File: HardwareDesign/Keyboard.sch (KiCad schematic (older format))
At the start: 13 parts, among them J501 Conn_01x20, U501 87C51/89C51, U502 IDT7201, U503 74HCT138, U504 74HCT541, Y501 11.0592 MHz

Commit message: more preparations for PCB layout
More nets connected to appropriate backplane connector pin.
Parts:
- removed RN501: 4k7, Resistors_THT:R_Array_SIP10, symbol device:R_Network09
- added J502: Conn_02x40_Counter_Clockwise, symbol Connector_Generic:Conn_02x40_Counter_Clockwise
- added J503: Conn_01x02, symbol Connector_Generic:Conn_01x02
- added RN501: R_Network08, Resistors_THT:R_Array_SIP9, symbol device:R_Network08
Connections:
- net labels added: A1, A10, A11, A12, A13, A14, A15, A2, A3, A4, A5, A6, A7, A8, A9, E, PC0, PC1, PC2, PC3, PC4, PC5, PC6, PC7, R~W, TIRQ, ~IODEV0, ~IODEV1, ~IODEV10, ~IODEV11, ~IODEV12, ~IODEV13, ~IODEV14, ~IODEV15, ~IODEV2, ~IODEV3, ~IODEV4, ~IODEV5, ~IODEV6, ~IODEV7, ~IODEV8, ~IODEV9, ~IOR1~, ~IOR2~, ~IOR3~, ~IOR4~, ~IOR5~, ~IOR6~, ~IOR7~, ~IRQ, ~KIRQ~, ~RMEM~, ~ROMEN~, ~RST~, ~WMEM~
- wire segments 174 -> 261
- no-connect marks 5 -> 4
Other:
- note added: "Jumper to enable keyboard\nIRQ (when FIFO is not empty)"
- note added: "The exact value of RN501 isn't\ncritical: anything between 2k7\nand 47k should work fine."
- note added: "back row (backplane)\nbottom row (board)"
- note added: "backplane connector"
- note added: "front row (backplane)\ntop row (board)"
- note removed: "Note that RN501 could also be\na 9 pin (8 resistor) network.\nThe exact value isn't critical:\nanything between 2k7 and 47k\nshould work fine."
- moved on the sheet: C501, C502, C503, C504, C505, C506, J501, U501, U502, U503, U504, Y501

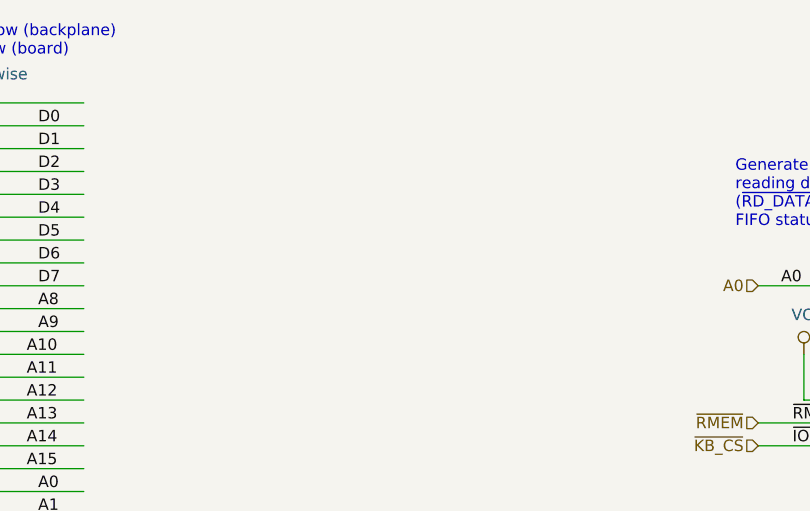
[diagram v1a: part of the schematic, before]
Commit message: more preparations for PCB layout
Make sure all nets connected to backplane connector pins are
labeled correctly.

Add bulk decoupling caps for each backplane connector.

Make keyboard interrupt be -IRQ5 rather than -IRQ7.
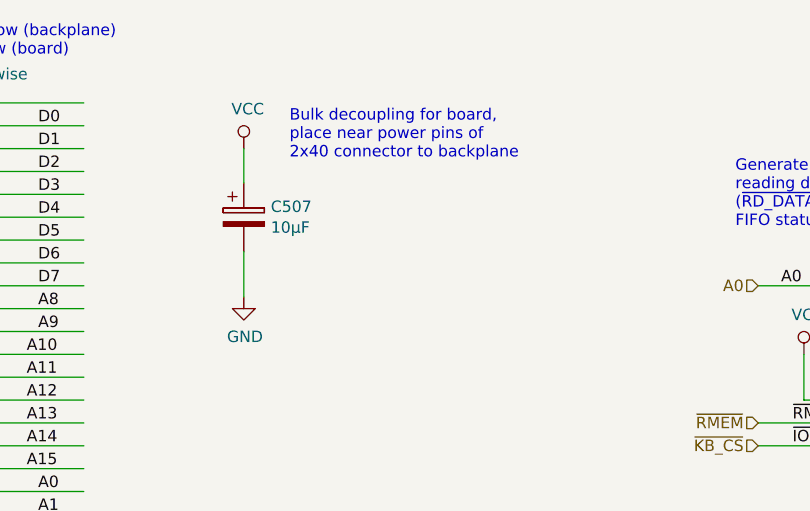
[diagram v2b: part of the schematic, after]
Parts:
- added C507: 10μF, symbol device:CP
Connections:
- wire segments 261 -> 263
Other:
- note added: "Bulk decoupling for board,\nplace near power pins of\n2x40 connector to backplane"
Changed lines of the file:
@@
 Text Label 10850 1250 0    50   ~ 0
 ~KIRQ~
+Text HLabel 11350 1250 2    50   Output ~ 0
+~KIRQ~
+Text Notes 10300 900  0    50   ~ 0
+Jumper to enable keyboard\nIRQ (when FIFO is not empty)
+$Comp
+L device:CP C?
+U 1 1 60CF49C0
+P 3200 1400
+AR Path="/5CFA6AAA/60CF49C0" Ref="C?"  Part="1"
+AR Path="/5E2CF983/60CF49C0" Ref="C507"  Part="1"
+F 0 "C507" H 3318 1446 50  0000 L CNN
+F 1 "10μF" H 3318 1355 50  0000 L CNN
+F 2 "" H 3238 1250 50  0001 C CNN
+F 3 "" H 3200 1400 50  0001 C CNN
+	1    3200 1400
+	1    0    0    -1
+$EndComp
+Wire Wire Line
+	3200 1250 3200 1100
+$Comp
+L power:VCC #PWR?
+U 1 1 60CF49C7
+P 3200 1100
+F 0 "#PWR?" H 3200 950 50  0001 C CNN
+F 1 "VCC" H 3217 1273 50  0000 C CNN
+F 2 "" H 3200 1100 50  0001 C CNN
+F 3 "" H 3200 1100 50  0001 C CNN
+	1    3200 1100
+	1    0    0    -1
+$EndComp
+Wire Wire Line
+	3200 1550 3200 1750
+$Comp
+L power:GND #PWR?
+U 1 1 60CF49CE
+P 3200 1750
+F 0 "#PWR?" H 3200 1500 50  0001 C CNN
+F 1 "GND" H 3205 1577 50  0000 C CNN
+F 2 "" H 3200 1750 50  0001 C CNN
+F 3 "" H 3200 1750 50  0001 C CNN
+	1    3200 1750
+	1    0    0    -1
+$EndComp
+Text Notes 3400 1150 0    50   ~ 0
+Bulk decoupling for board,\nplace near power pins of\n2x40 connector to backplane
 Wire Bus Line
 	8250 1950 8250 5300
 Wire Bus Line
 	10900 1950 10900 6950
-Text HLabel 11350 1250 2    50   Output ~ 0
-~KIRQ~
-Text Notes 10300 900  0    50   ~ 0
-Jumper to enable keyboard\nIRQ (when FIFO is not empty)
 $EndSCHEMATC

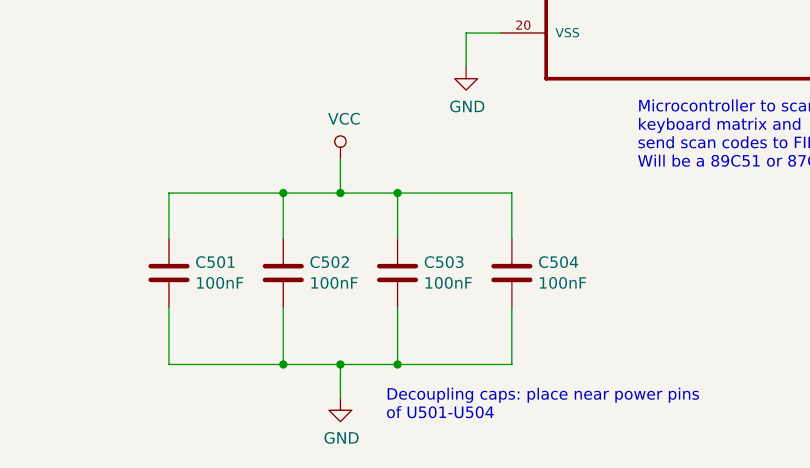
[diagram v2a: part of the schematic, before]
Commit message: a few more consistency tweaks before PCB layout
Routed second timer/counter output to backplane connector,
just in case we want to use it for something eventually
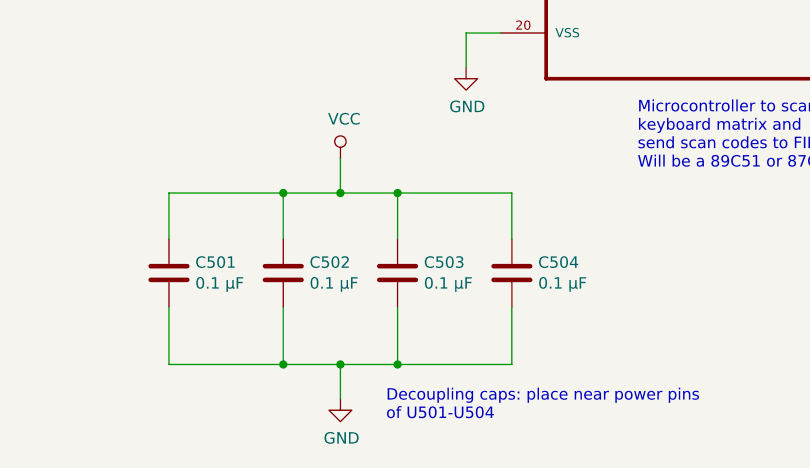
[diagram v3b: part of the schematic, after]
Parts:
- C501, C502, C503, C504: value 100nF -> 0.1 μF
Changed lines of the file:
@@
 P 3450 7950
 F 0 "C501" H 3565 7996 50  0000 L CNN
-F 1 "100nF" H 3565 7905 50  0000 L CNN
+F 1 "0.1 μF" H 3565 7905 50  0000 L CNN
 F 2 "" H 3488 7800 50  0001 C CNN
 F 3 "" H 3450 7950 50  0001 C CNN
@@
 P 3950 7950
 F 0 "C502" H 4065 7996 50  0000 L CNN
-F 1 "100nF" H 4065 7905 50  0000 L CNN
+F 1 "0.1 μF" H 4065 7905 50  0000 L CNN
 F 2 "" H 3988 7800 50  0001 C CNN
 F 3 "" H 3950 7950 50  0001 C CNN
@@
 P 4450 7950
 F 0 "C503" H 4565 7996 50  0000 L CNN
-F 1 "100nF" H 4565 7905 50  0000 L CNN
+F 1 "0.1 μF" H 4565 7905 50  0000 L CNN
 F 2 "" H 4488 7800 50  0001 C CNN
 F 3 "" H 4450 7950 50  0001 C CNN
@@
 P 4950 7950
 F 0 "C504" H 5065 7996 50  0000 L CNN
-F 1 "100nF" H 5065 7905 50  0000 L CNN
+F 1 "0.1 μF" H 5065 7905 50  0000 L CNN
 F 2 "" H 4988 7800 50  0001 C CNN
 F 3 "" H 4950 7950 50  0001 C CNN
@@
 U 1 1 60CF49C7
 P 3200 1100
+AR Path="/5CFA6AAA/60CF49C7" Ref="#PWR?"  Part="1"
+AR Path="/5E2CF983/60CF49C7" Ref="#PWR?"  Part="1"
 F 0 "#PWR?" H 3200 950 50  0001 C CNN
 F 1 "VCC" H 3217 1273 50  0000 C CNN
@@
 U 1 1 60CF49CE
 P 3200 1750
+AR Path="/5CFA6AAA/60CF49CE" Ref="#PWR?"  Part="1"
+AR Path="/5E2CF983/60CF49CE" Ref="#PWR?"  Part="1"
 F 0 "#PWR?" H 3200 1500 50  0001 C CNN
 F 1 "GND" H 3205 1577 50  0000 C CNN

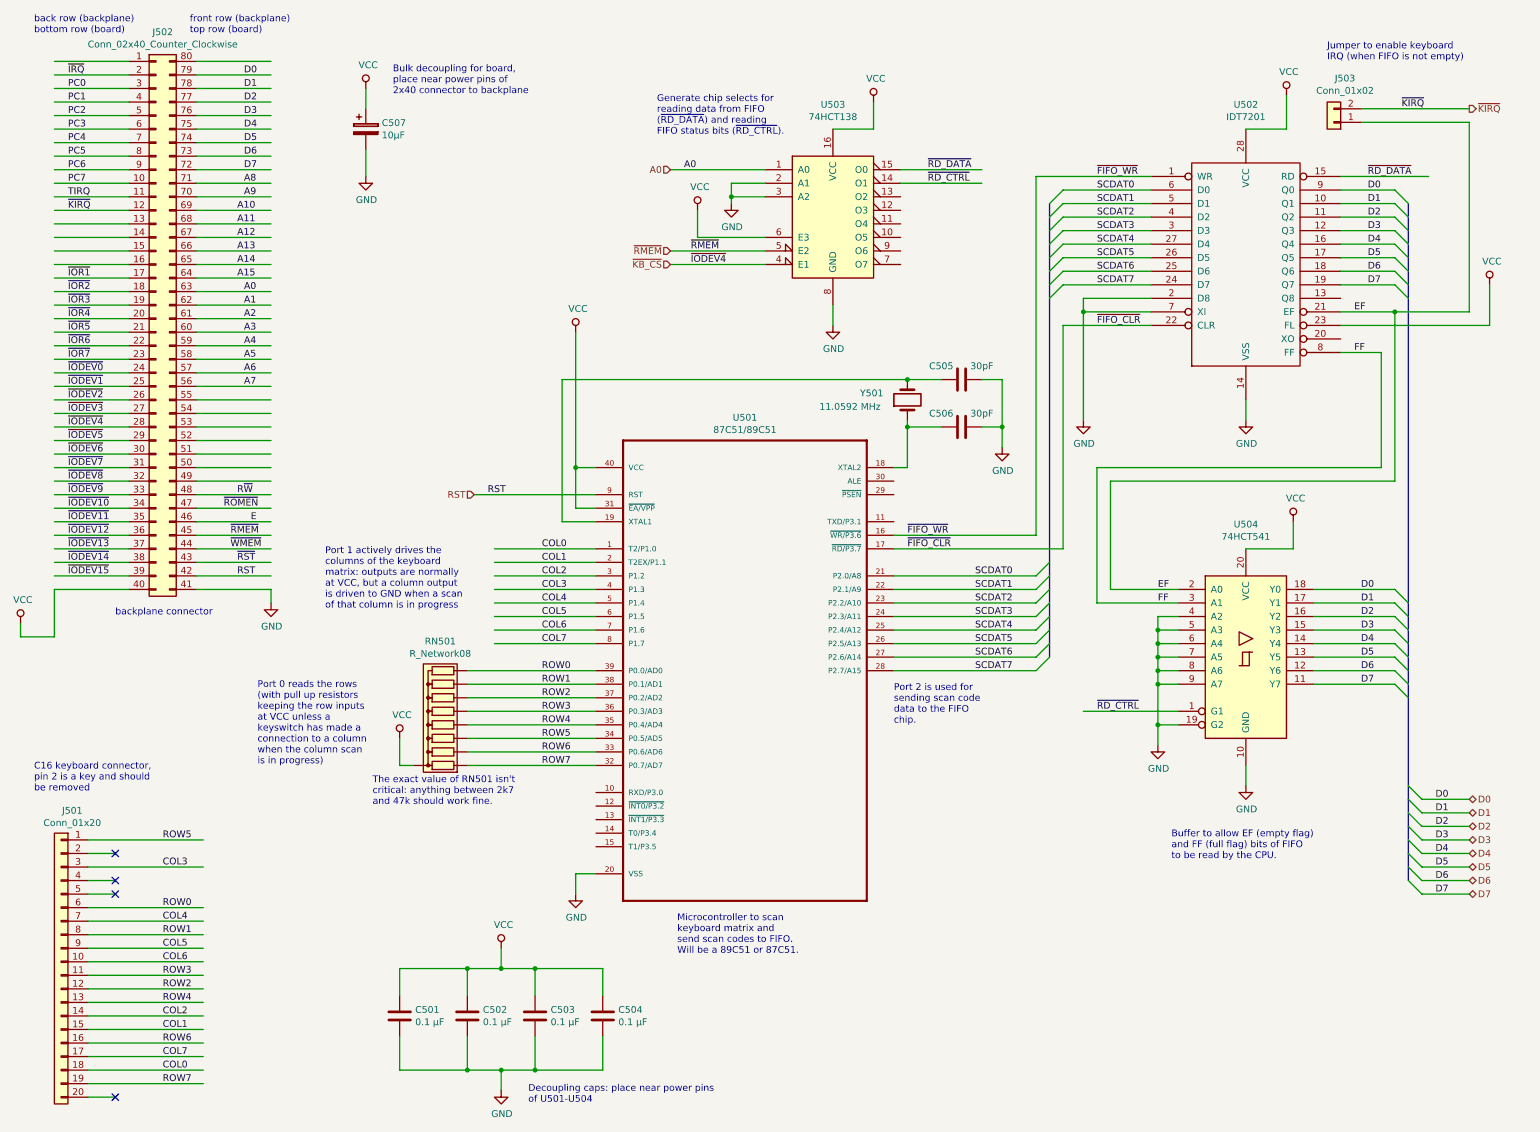
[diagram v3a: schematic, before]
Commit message: have one copy of backplane connector on main sheet
Avoids need to replicate it elsewhere, and helps ensure
that all signals are connected correctly.
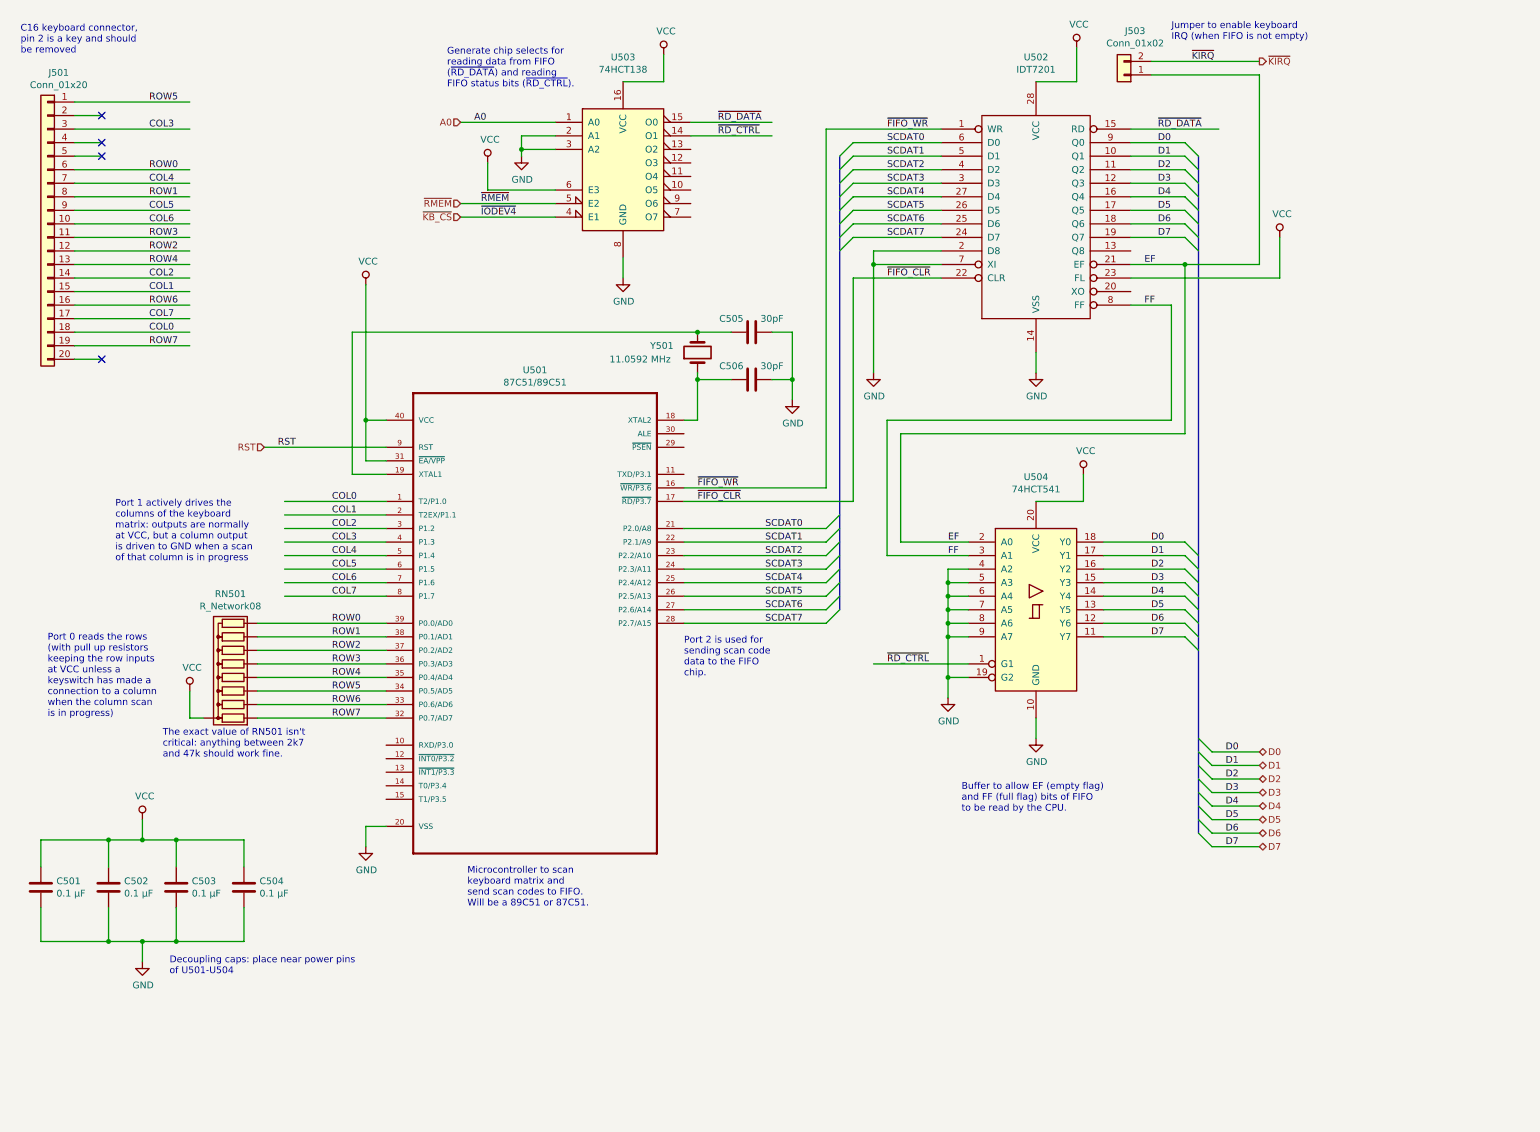
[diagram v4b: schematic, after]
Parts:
- removed C507: 10μF, symbol device:CP
- removed J502: Conn_02x40_Counter_Clockwise, symbol Connector_Generic:Conn_02x40_Counter_Clockwise
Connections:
- net labels removed: A1, A10, A11, A12, A13, A14, A15, A2, A3, A4, A5, A6, A7, A8, A9, E, PC0, PC1, PC2, PC3, PC4, PC5, PC6, PC7, R~W, TIRQ, ~IODEV0, ~IODEV1, ~IODEV10, ~IODEV11, ~IODEV12, ~IODEV13, ~IODEV14, ~IODEV15, ~IODEV2, ~IODEV3, ~IODEV5, ~IODEV6, ~IODEV7, ~IODEV8, ~IODEV9, ~IOR1~, ~IOR2~, ~IOR3~, ~IOR4~, ~IOR5~, ~IOR6~, ~IOR7~, ~IRQ, ~ROMEN~, ~RST~, ~WMEM~
- wire segments 263 -> 177
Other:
- note removed: "Bulk decoupling for board,\nplace near power pins of\n2x40 connector to backplane"
- note removed: "back row (backplane)\nbottom row (board)"
- note removed: "backplane connector"
- note removed: "front row (backplane)\ntop row (board)"
- moved on the sheet: C501, C502, C503, C504, C505, C506, J501, J503, RN501, U501, U502, U503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
